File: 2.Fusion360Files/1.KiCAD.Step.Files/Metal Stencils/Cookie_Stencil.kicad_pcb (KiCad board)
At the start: 2 copper layers, 61 x 22.6 mm, 0 parts

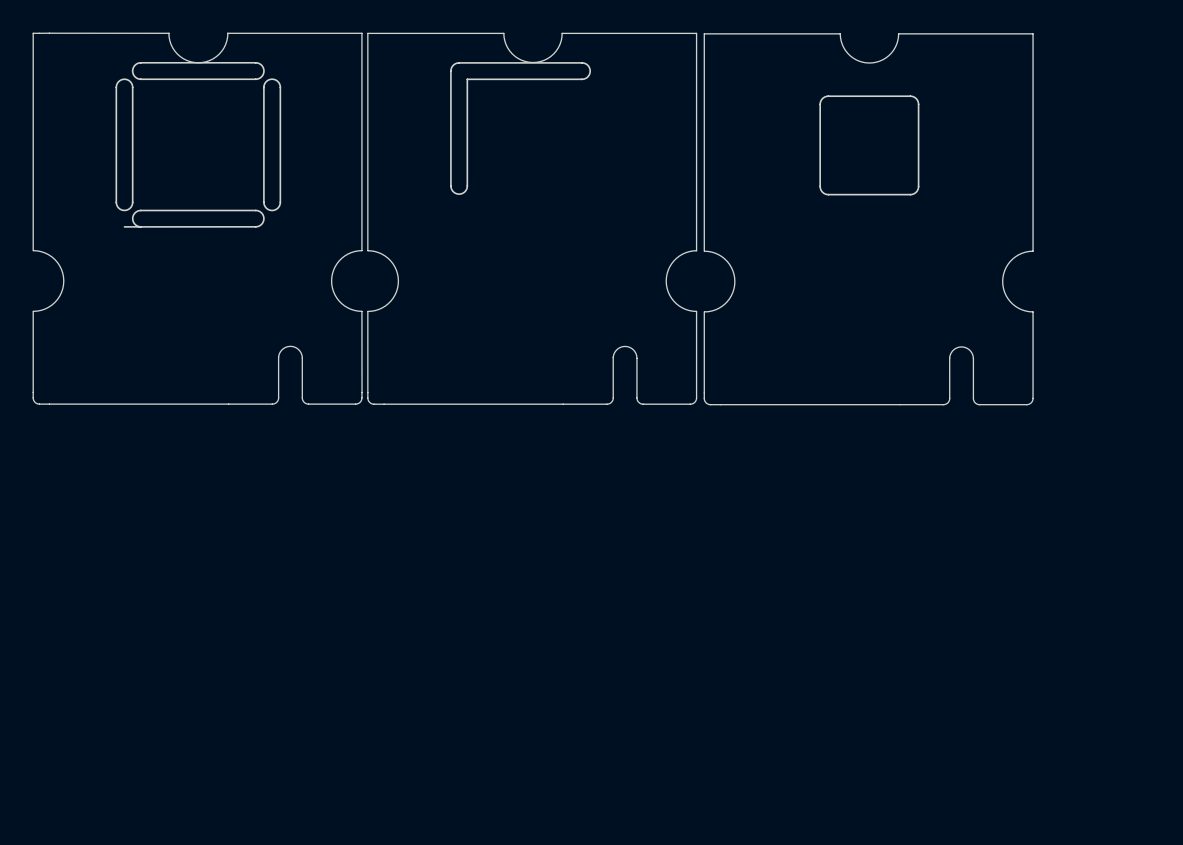
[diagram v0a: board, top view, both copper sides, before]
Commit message: Updated to blind vias
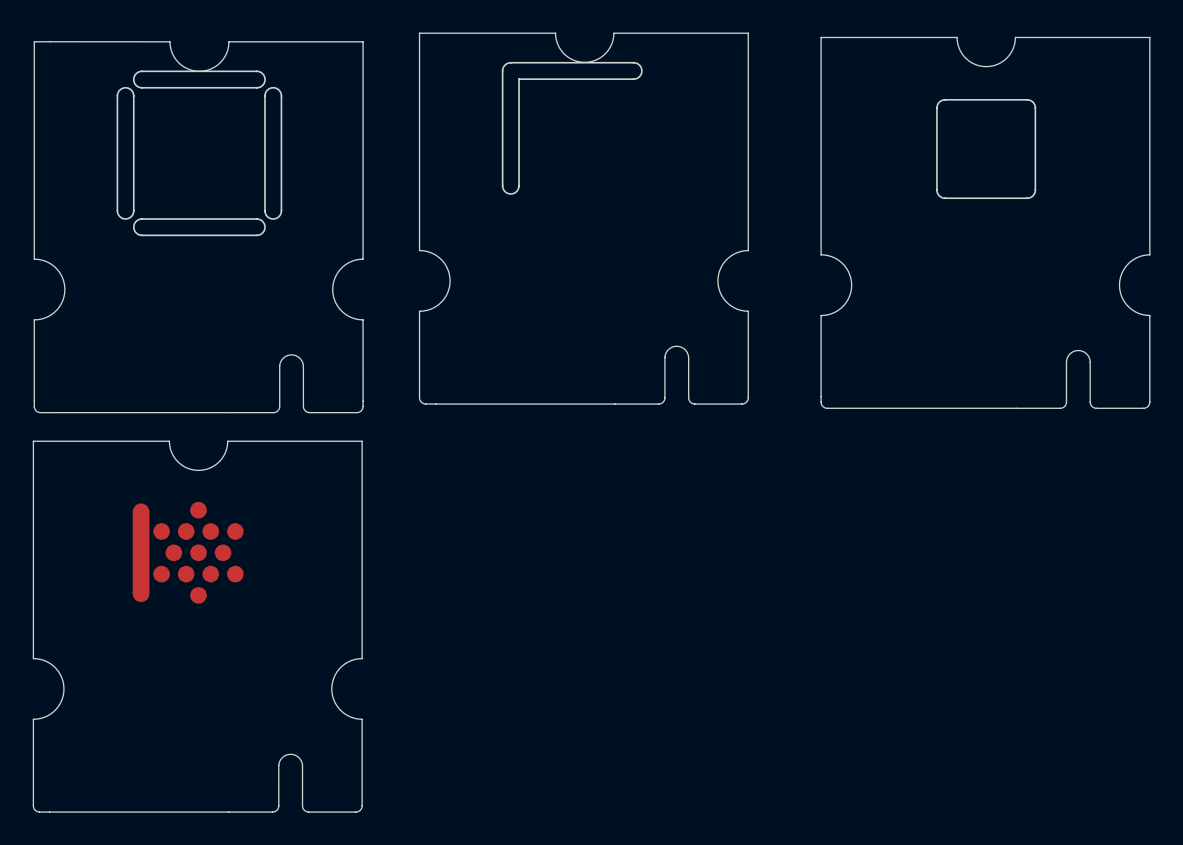
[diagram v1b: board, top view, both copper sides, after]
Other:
- board size 61 x 22.6 mm -> 68.1 x 47.5 mm
